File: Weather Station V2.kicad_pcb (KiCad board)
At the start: 4 copper layers, 123.5 x 67.3 mm, 64 parts, among them J1 SOLAR IN, J10 SP13 Socket, J2 18650, J3 Battery_AUX, J4 Conn_01x08_Socket, J5 Conn_01x08_Socket, J6 USB_C, J7 RYLR998, J8 Breakout, J9 SP13 Socket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

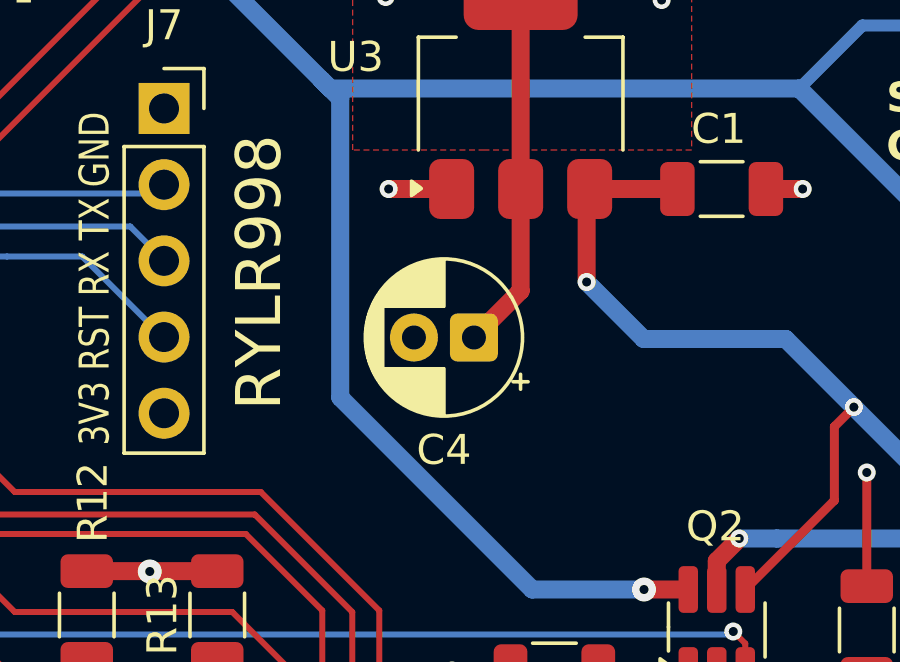
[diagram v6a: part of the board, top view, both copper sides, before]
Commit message: - Changed 3V3 LDO to LDL1117S33R - In a previous commit ON OFF power lables were switched
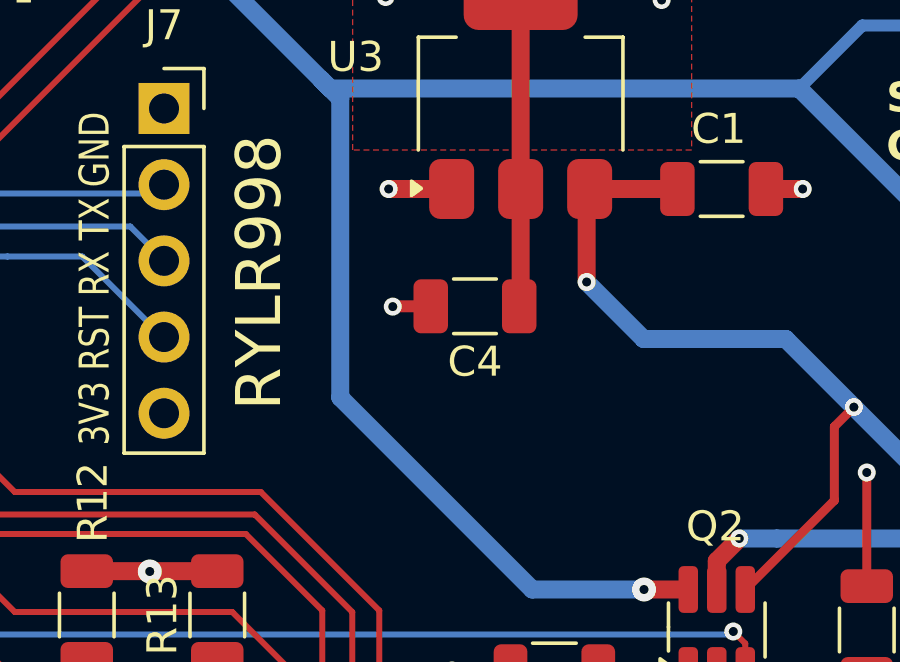
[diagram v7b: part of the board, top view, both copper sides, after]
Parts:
- C4: value 10uF -> 4.7uF; footprint Capacitor_THT:CP_Radial_D5.0mm_P2.00mm -> Capacitor_SMD:C_1206_3216Metric
- U3: value LM1117MP-3.3 -> LDL1117S33R
- moved C4 1.04 mm to (128.9, 94.5)
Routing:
- net +3V3: track 83.5 -> 81.9 mm
- net GND: track 34.8 -> 36.1 mm, vias 17 -> 18
